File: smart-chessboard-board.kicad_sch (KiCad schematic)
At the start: 7 parts, among them J101 Conn_01x12_MountingPin

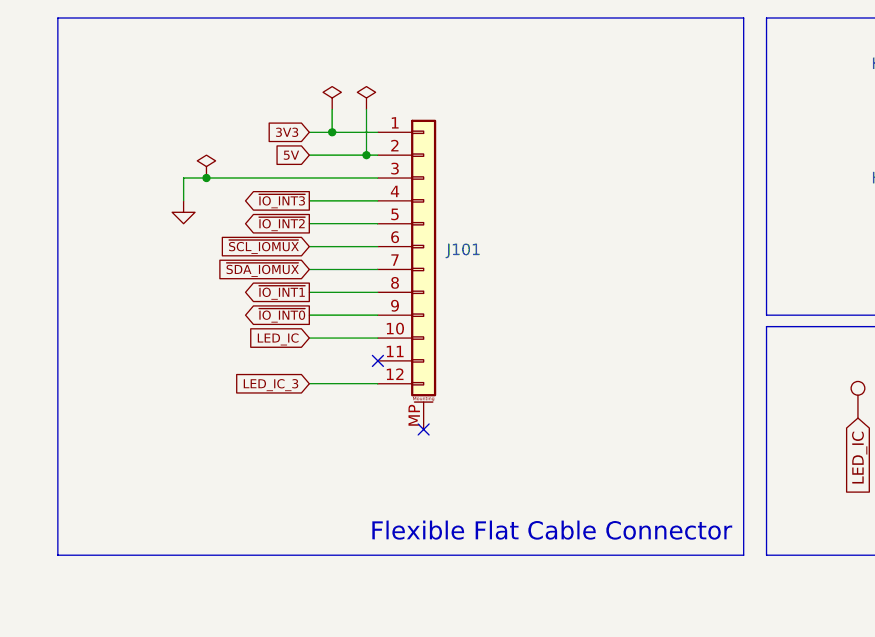
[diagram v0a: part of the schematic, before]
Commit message: fix issues in rev.b design
- fix connector design to fix potential crosstalk issues with LED data line causing unintentional LED light in the first LED in the array.
- combined all interrupts into single interrupt.
- add ground between each connector pin (to rid crosstalk).
- added in-line resistor to minimize crosstalk (33 ohms)
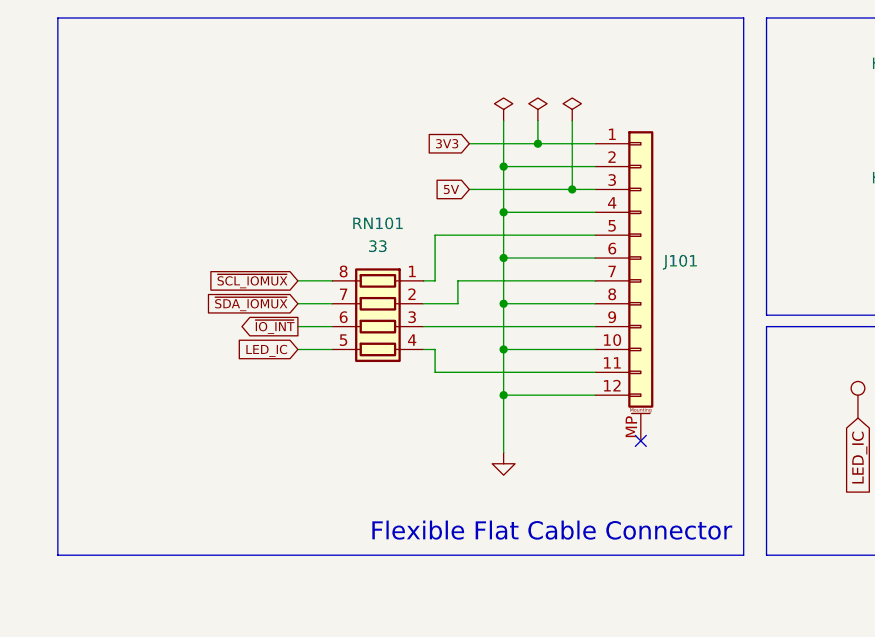
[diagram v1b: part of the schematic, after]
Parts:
- added RN101: 33, Resistor_SMD:R_Array_Convex_4x0603, symbol Device:R_Pack04
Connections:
- net LED_IC_3 is gone; now on net GND: J101.12 (Pin_12)
- net ~{IO_INT1} is gone; now on net GND: J101.8 (Pin_8)
- net ~{IO_INT3} is gone; now on net GND: J101.4 (Pin_4)
- net 5V: now also J101.3 (Pin_3); no longer J101.2 (Pin_2)
- net GND: now also J101.10 (Pin_10), J101.2 (Pin_2), J101.6 (Pin_6); no longer J101.3 (Pin_3)
- net LED_IC: now also RN101.5 (R4.2); no longer J101.10 (Pin_10)
- net ~{SCL_IOMUX}: now also RN101.8 (R1.2); no longer J101.6 (Pin_6)
- net ~{SDA_IOMUX}: now also RN101.7 (R2.2); no longer J101.7 (Pin_7)
- net at J101.11 (Pin_11): now also RN101.4 (R4.1)
- net ~{IO_INT0}: no longer names the net of J101.9 (Pin_9)
- net ~{IO_INT0}: now also RN101.3 (R3.1)
- net ~{IO_INT2}: no longer names the net of J101.5 (Pin_5)
- net ~{IO_INT2}: now also RN101.1 (R1.1)
- new net: J101.7 (Pin_7), RN101.2 (R2.1)
- new net ~{IO_INT}: RN101.6 (R3.2)
- no-connect marks 6 -> 5
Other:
- moved on the sheet: J101

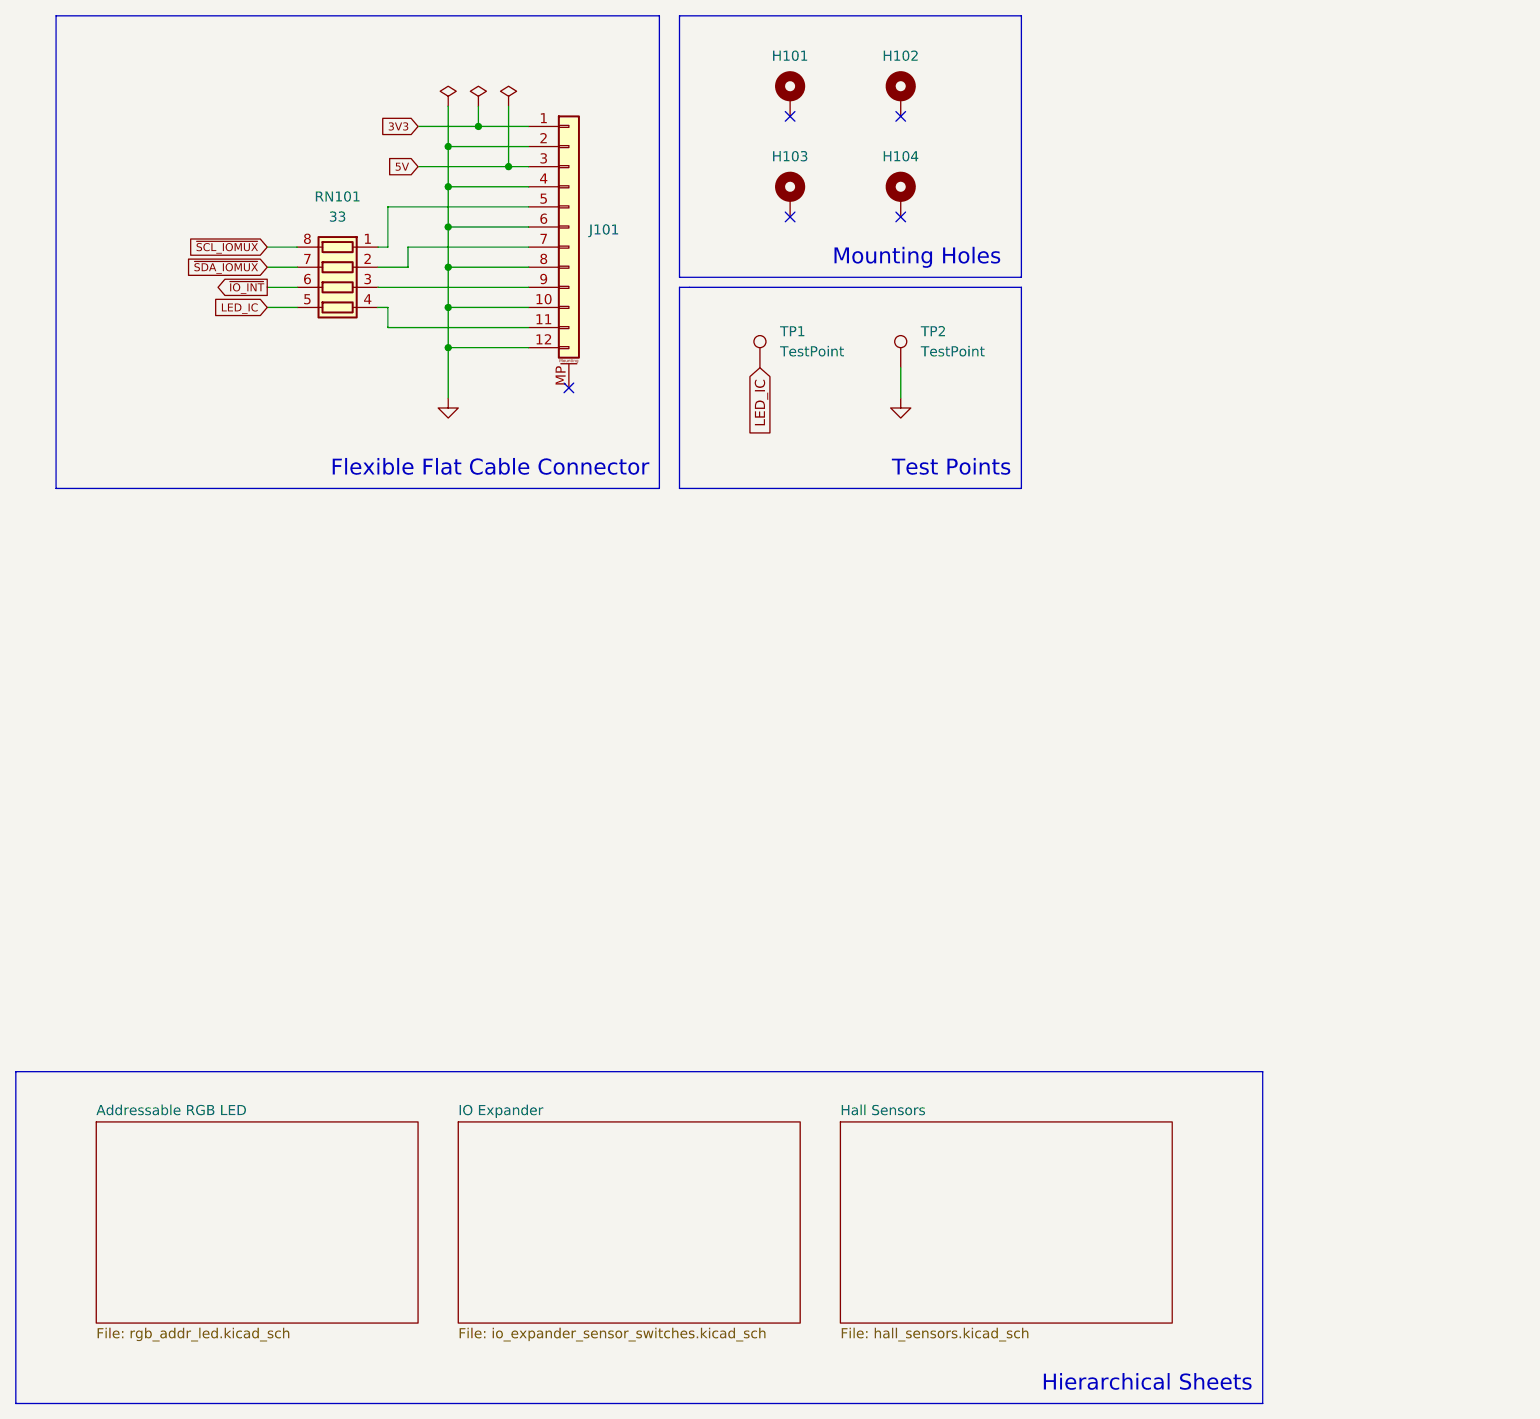
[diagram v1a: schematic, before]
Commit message: add ambient light sensor
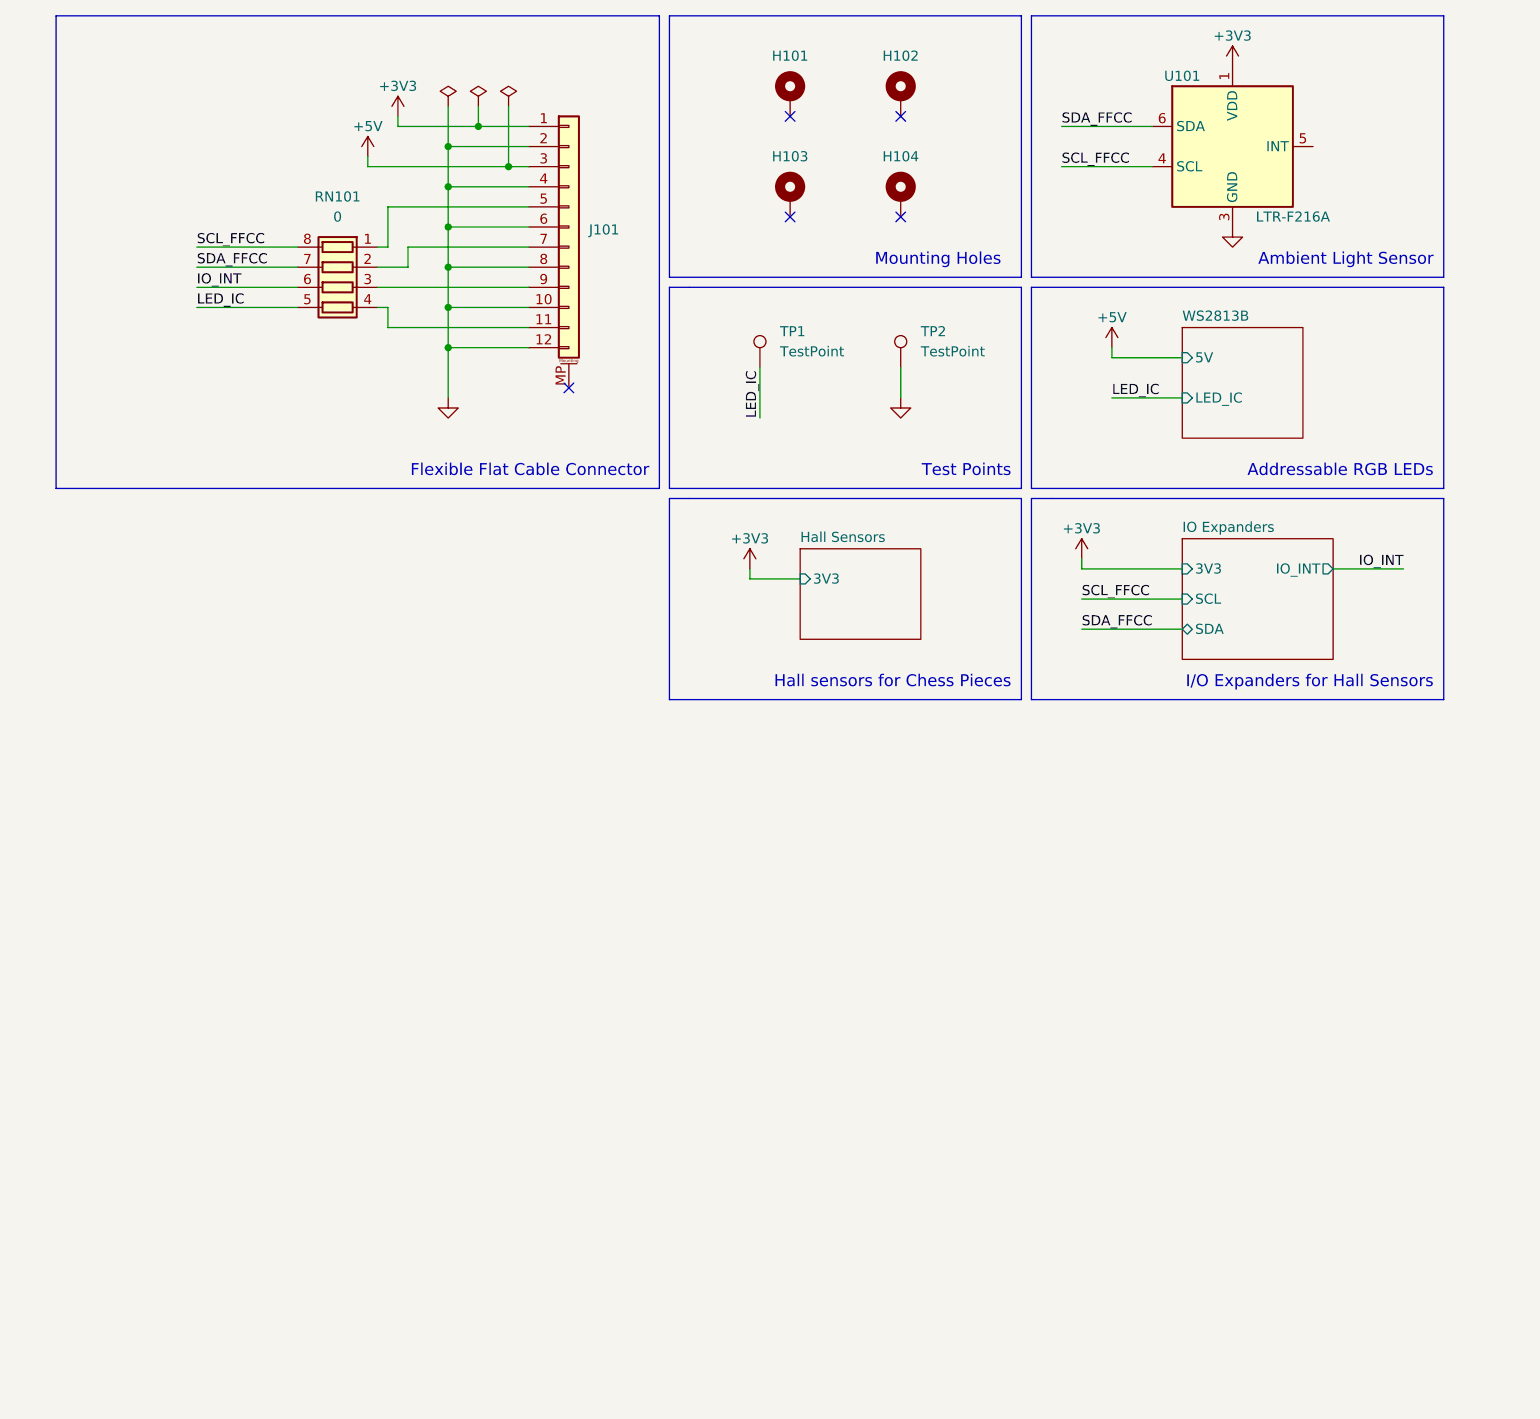
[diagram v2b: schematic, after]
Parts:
- added U101: LTR-F216A, OptoDevice:Lite-On_LTR-303ALS-01, symbol Sensor_Optical:LTR-303ALS-01
- RN101: value 33 -> 0; LCSC C169805 -> C327053
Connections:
- net GND: now also U101.3 (GND)
- net 3V3 renamed +3V3
- net +3V3: now also U101.1 (VDD)
- net 5V renamed +5V
- net ~{IO_INT} renamed IO_INT
- net ~{SCL_IOMUX} renamed SCL_FFCC
- net SCL_FFCC: now also U101.4 (SCL)
- net ~{SDA_IOMUX} renamed SDA_FFCC
- net SDA_FFCC: now also U101.6 (SDA)
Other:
- sheet Addressable RGB LED renamed WS2813B
- sheet IO Expander renamed IO Expanders
- sheet Hall Sensors ports: added 3V3; removed none
- sheet IO Expanders ports: added 3V3, IO_INT, SCL, SDA; removed none
- sheet WS2813B ports: added 5V, LED_IC; removed none
- note added: "Addressable RGB LEDs"
- note added: "Ambient Light Sensor"
- note added: "Hall sensors for Chess Pieces"
- note added: "I/O Expanders for Hall Sensors"
- note removed: "Hierarchical Sheets"

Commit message: add bus buffer
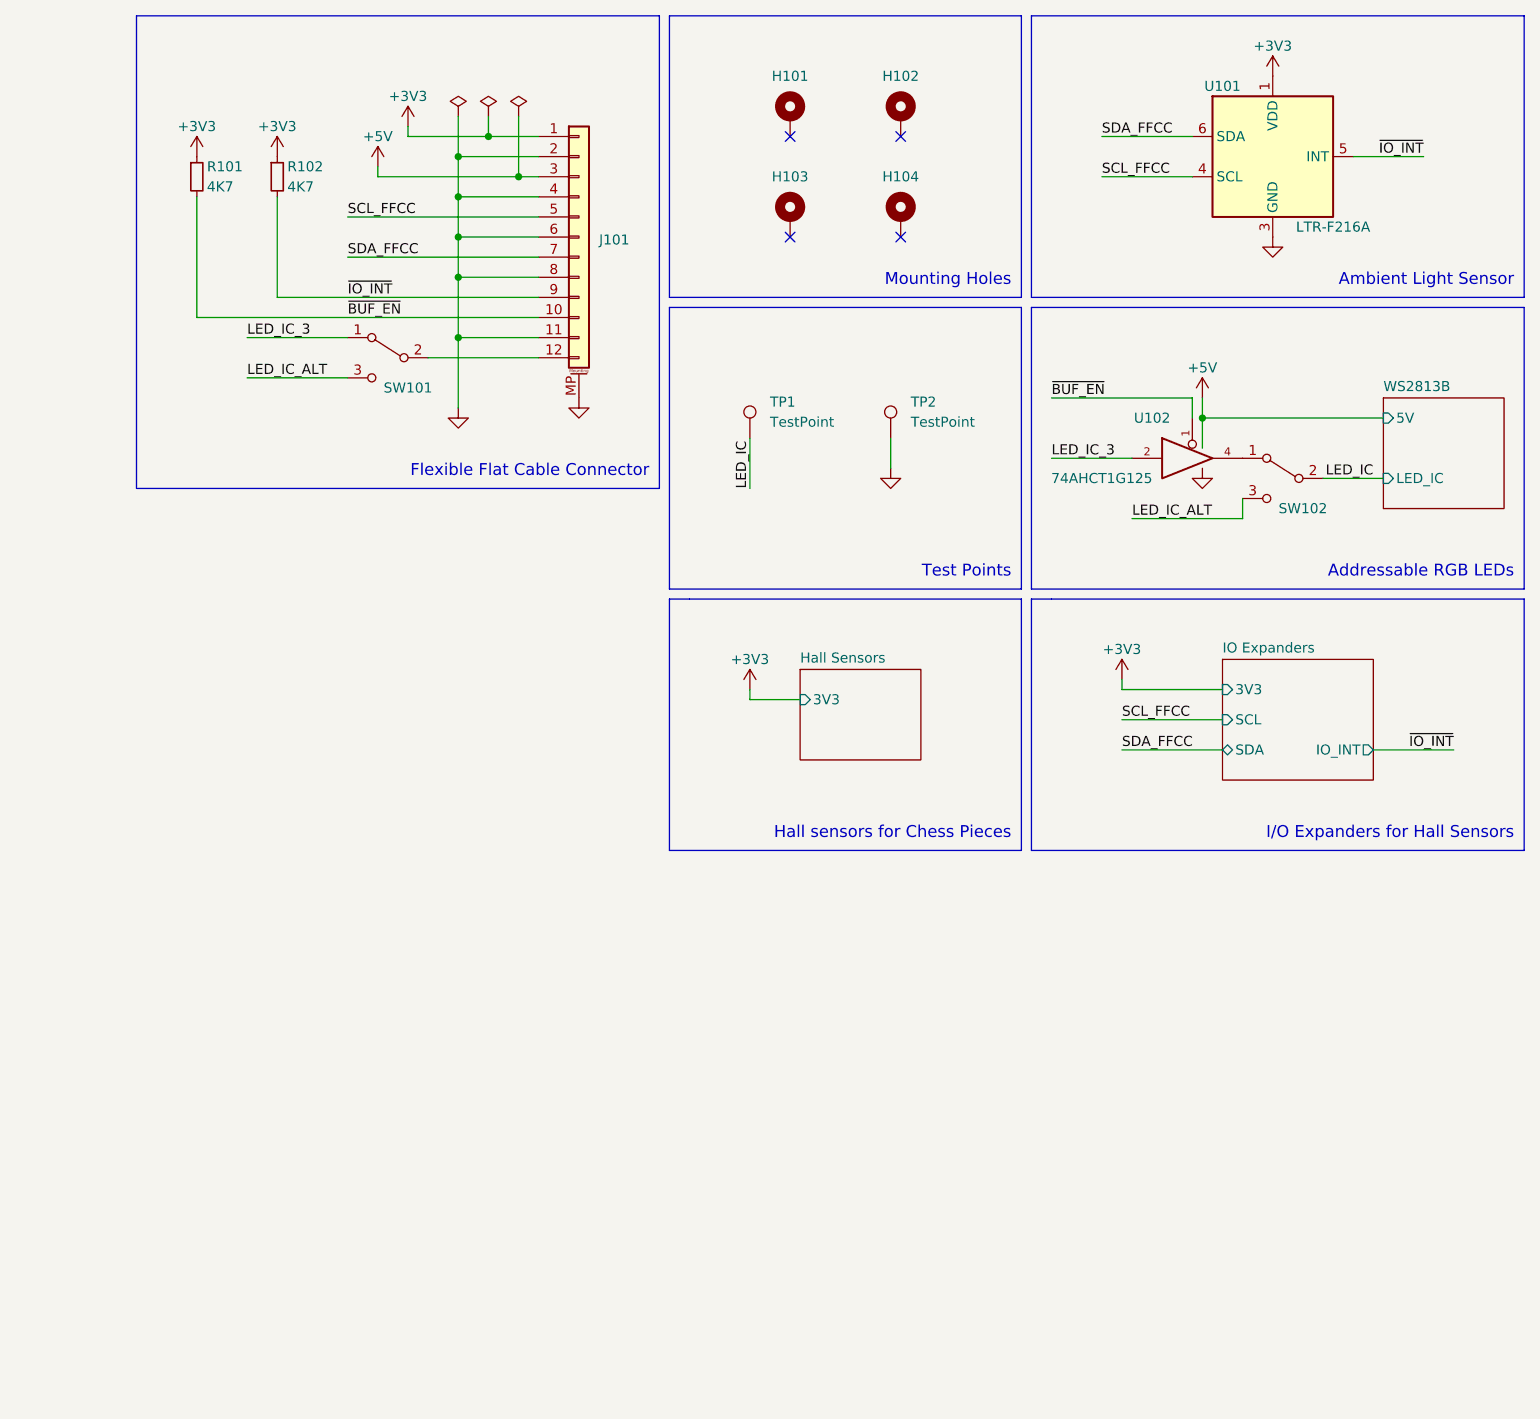
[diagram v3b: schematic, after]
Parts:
- removed RN101: 0, Resistor_SMD:R_Array_Convex_4x0603, symbol Device:R_Pack04
- added R101, R102: 4K7, Resistor_SMD:R_0603_1608Metric, symbol Device:R_Small
- added SW101, SW102: SW_SPDT, Jumper:SolderJumper-3_P2.0mm_Open_TrianglePad1.0x1.5mm, symbol Switch:SW_SPDT
- added U102: 74AHCT1G125, Package_TO_SOT_SMD:SOT-23-5, symbol 74xGxx:74AHCT1G125
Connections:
- net +3V3: now also R101.1, R102.1
- net +5V: now also U102.5 (VCC)
- net GND: now also J101.11 (Pin_11), J101.MP (MountPin), U102.3 (GND); no longer J101.10 (Pin_10), J101.12 (Pin_12)
- net LED_IC: now also SW102.2 (B)
- net SCL_FFCC: now also J101.5 (Pin_5)
- net SDA_FFCC: now also J101.7 (Pin_7)
- net ~{IO_INT}: now reaches U101.5 (INT)
- net ~{IO_INT}: now also J101.9 (Pin_9), R102.2
- new net: SW102.1 (A), U102.4
- new net: J101.12 (Pin_12), SW101.2 (B)
- new net LED_IC_3: SW101.1 (A), U102.2
- new net LED_IC_ALT: SW101.3 (C), SW102.3 (C)
- new net ~{BUF_EN}: J101.10 (Pin_10), R101.2, U102.1
- no-connect marks 5 -> 4
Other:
- moved on the sheet: H101, H102, H103, H104, J101, TP1, TP2, U101
